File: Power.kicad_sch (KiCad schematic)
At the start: 1 part, among them J901 Conn_01x02

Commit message: Fix schematic ERC errors
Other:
- sheet Supercaps ports: added Vscap; removed Vcap
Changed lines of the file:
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@@
 		)
 	)
-	(hierarchical_label "Vcap"
+	(hierarchical_label "Vscap"
 		(shape output)
 		(at 146.05 31.75 0)
@@
 			)
 		)
-		(property "Sim.Enable" ""
-			(at 34.29 39.37 0)
-			(effects
-				(font
-					(size 1.27 1.27)
-				)
-			)
-		)
 		(pin "1"
 		)
@@
 			)
 		)
-		(pin "Vcap" bidirectional
+		(pin "Vscap" bidirectional
 			(at 143.51 68.58 180)
 			(effects

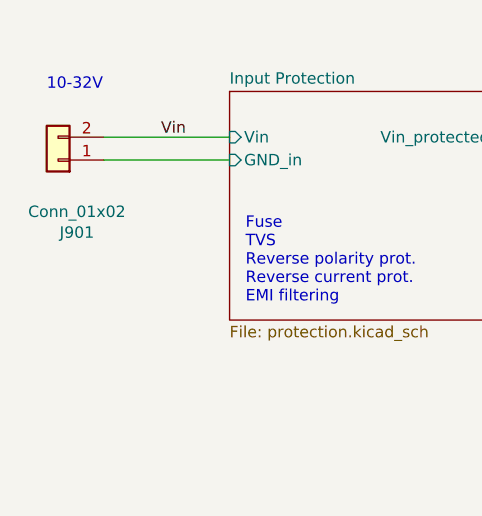
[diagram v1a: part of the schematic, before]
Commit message: Reannotate components
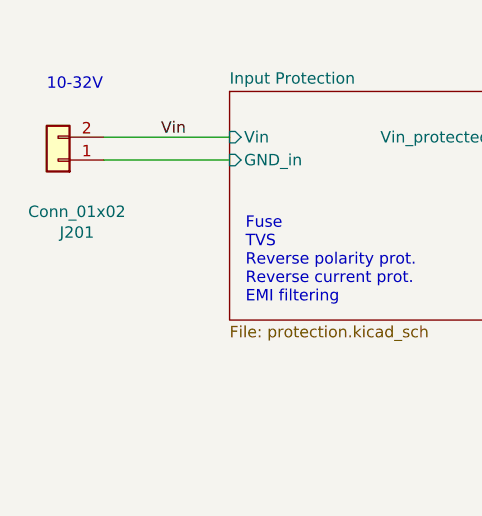
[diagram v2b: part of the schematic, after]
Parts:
- renumbered J901 to J201
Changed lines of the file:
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@@
 		(on_board yes)
 		(dnp no)
-		(property "Reference" "#PWR0901"
+		(property "Reference" "#PWR0201"
 			(at 215.9 36.83 0)
 			(effects
@@
 			(project "Yellow"
 				(path "/abc482bd-3f17-4d35-80db-1da3dcdb5c27/c7bf4e1f-6bd1-4be7-9e56-1bd438bf5d42"
-					(reference "#PWR0901")
+					(reference "#PWR0201")
 					(unit 1)
 				)
@@
 		(on_board yes)
 		(dnp no)
-		(property "Reference" "J901"
+		(property "Reference" "J201"
 			(at 36.3728 47.4218 0)
 			(effects
@@
 			(project "Yellow"
 				(path "/abc482bd-3f17-4d35-80db-1da3dcdb5c27/c7bf4e1f-6bd1-4be7-9e56-1bd438bf5d42"
-					(reference "J901")
+					(reference "J201")
 					(unit 1)
 				)
@@
 		(dnp no)
 		(fields_autoplaced yes)
-		(property "Reference" "#PWR0902"
+		(property "Reference" "#PWR0202"
 			(at 215.9 69.85 0)
 			(effects
@@
 			(project ""
 				(path "/abc482bd-3f17-4d35-80db-1da3dcdb5c27/c7bf4e1f-6bd1-4be7-9e56-1bd438bf5d42"
-					(reference "#PWR0902")
+					(reference "#PWR0202")
 					(unit 1)
 				)
@@
 			(project "HALPI2"
 				(path "/abc482bd-3f17-4d35-80db-1da3dcdb5c27/c7bf4e1f-6bd1-4be7-9e56-1bd438bf5d42"
-					(page "14")
+					(page "5")
 				)
 			)
@@
 			(project "HALPI2"
 				(path "/abc482bd-3f17-4d35-80db-1da3dcdb5c27/c7bf4e1f-6bd1-4be7-9e56-1bd438bf5d42"
-					(page "15")
+					(page "10")
 				)
 			)
@@
 			(project "HALPI2"
 				(path "/abc482bd-3f17-4d35-80db-1da3dcdb5c27/c7bf4e1f-6bd1-4be7-9e56-1bd438bf5d42"
-					(page "13")
+					(page "4")
 				)
 			)
@@
 			(project "HALPI2"
 				(path "/abc482bd-3f17-4d35-80db-1da3dcdb5c27/c7bf4e1f-6bd1-4be7-9e56-1bd438bf5d42"
-					(page "12")
+					(page "3")
 				)
 			)
@@
 			(project "HALPI2"
 				(path "/abc482bd-3f17-4d35-80db-1da3dcdb5c27/c7bf4e1f-6bd1-4be7-9e56-1bd438bf5d42"
-					(page "16")
-				)
-			)
+					(page "11")
+				)
+			)

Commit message: Further refinements
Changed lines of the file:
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@@
 		)
 	)
-	(hierarchical_label "EN5V"
+	(hierarchical_label "VCCEN"
 		(shape input)
 		(at 184.15 73.66 180)
@@
 		)
 	)
-	(hierarchical_label "EN5V"
+	(hierarchical_label "VCCEN"
 		(shape input)
 		(at 184.15 40.64 180)
@@
 			)
 		)
+		(property "LCSC Part" ""
+			(at 34.29 39.37 0)
+			(effects
+				(font
+					(size 1.27 1.27)
+				)
+			)
+		)
+		(property "Sim.Enable" ""
+			(at 34.29 39.37 0)
+			(effects
+				(font
+					(size 1.27 1.27)
+				)
+			)
+		)

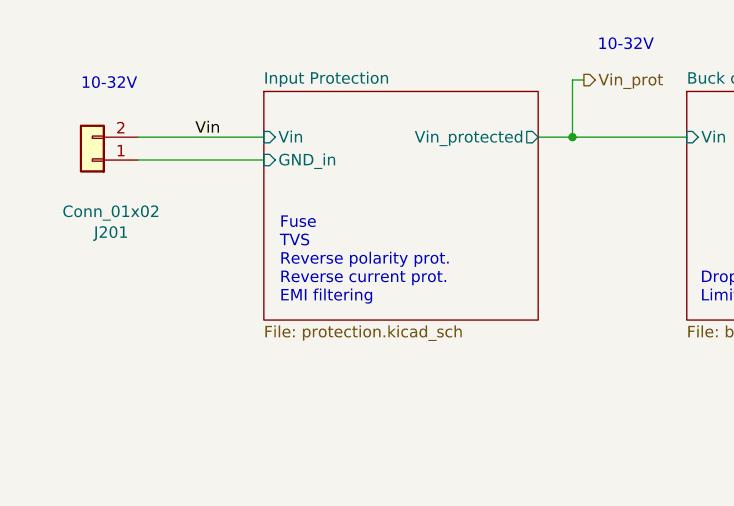
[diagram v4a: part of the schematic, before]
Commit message: Change MCU to RP2040
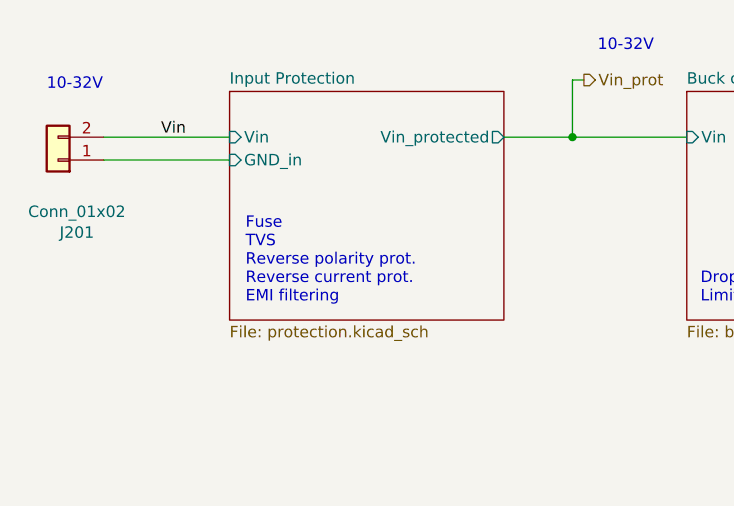
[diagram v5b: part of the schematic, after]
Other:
- moved on the sheet: J201
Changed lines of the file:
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@@
 	(text "10-32V"
 		(exclude_from_sim no)
-		(at 33.02 31.75 0)
+		(at 29.21 31.75 0)
 		(effects
 			(font
@@
 	(text "Fuse\nTVS\nReverse polarity prot.\nReverse current prot.\nEMI filtering"
 		(exclude_from_sim no)
-		(at 55.118 55.372 0)
+		(at 51.308 55.372 0)
 		(effects
 			(font
@@
 	(wire
 		(pts
-			(xy 39.37 36.83) (xy 53.34 36.83)
+			(xy 35.56 36.83) (xy 49.53 36.83)
 		)
 		(stroke
@@
 	(wire
 		(pts
-			(xy 83.82 36.83) (xy 87.63 36.83)
+			(xy 80.01 36.83) (xy 87.63 36.83)
 		)
 		(stroke
@@
 	(wire
 		(pts
-			(xy 39.37 39.37) (xy 53.34 39.37)
+			(xy 35.56 39.37) (xy 49.53 39.37)
 		)
 		(stroke
@@
 	)
 	(label "Vin"
-		(at 45.72 36.83 0)
+		(at 41.91 36.83 0)
 		(effects
 			(font
@@
 	(symbol
 		(lib_id "Connector_Generic:Conn_01x02")
-		(at 34.29 39.37 180)
+		(at 30.48 39.37 180)
 		(unit 1)
 		(exclude_from_sim no)
@@
 		(dnp no)
 		(property "Reference" "J201"
-			(at 36.3728 47.4218 0)
+			(at 32.5628 47.4218 0)
 			(effects
 				(font
@@
 		)
 		(property "Value" "Conn_01x02"
-			(at 36.3728 45.1104 0)
+			(at 32.5628 45.1104 0)
 			(effects
 				(font
@@
 		)
 		(property "Footprint" "Connector_Phoenix_MC:PhoenixContact_MCV_1,5_2-G-3.81_1x02_P3.81mm_Vertical"
-			(at 34.29 39.37 0)
+			(at 30.48 39.37 0)
 			(effects
 				(font
@@
 		)
 		(property "Datasheet" "~"
-			(at 34.29 39.37 0)
+			(at 30.48 39.37 0)
 			(effects
 				(font
@@
 		)
 		(property "Description" "Generic connector, single row, 01x02, script generated (kicad-library-utils/schlib/autogen/connector/)"
-			(at 34.29 39.37 0)
+			(at 30.48 39.37 0)
 			(effects
 				(font
@@
 		)
 		(property "LCSC" "C8396"
-			(at 34.29 39.37 0)
+			(at 30.48 39.37 0)
 			(effects
 				(font
@@
 		)
 		(property "JLCPCB_CORRECTION" ""
-			(at 34.29 39.37 0)
+			(at 30.48 39.37 0)
 			(effects
 				(font
@@
 		)
 		(property "Characteristics" ""
-			(at 34.29 39.37 0)
+			(at 30.48 39.37 0)
 			(effects
 				(font
@@
 		)
 		(property "LCSC Part" ""
-			(at 34.29 39.37 0)
+			(at 30.48 39.37 0)
 			(effects
 				(font
@@
 		)
 		(property "Sim.Enable" ""
-			(at 34.29 39.37 0)
+			(at 30.48 39.37 0)
 			(effects
 				(font
@@
 	)
 	(sheet
-		(at 53.34 31.75)
+		(at 49.53 31.75)
 		(size 30.48 25.4)
 		(exclude_from_sim no)
@@
 		)
 		(property "Sheetname" "Input Protection"
-			(at 53.34 31.0384 0)
+			(at 49.53 31.0384 0)
 			(effects
 				(font
@@
 		)
 		(property "Sheetfile" "protection.kicad_sch"
-			(at 53.34 57.7346 0)
+			(at 49.53 57.7346 0)
 			(effects
 				(font
@@
 		)
 		(pin "Vin_protected" output
-			(at 83.82 36.83 0)
+			(at 80.01 36.83 0)
 			(effects
 				(font
@@
 		)
 		(pin "Vin" input
-			(at 53.34 36.83 180)
+			(at 49.53 36.83 180)
 			(effects
 				(font
@@
 		)
 		(pin "GND_in" input
-			(at 53.34 39.37 180)
-			(effects
-				(font
+			(at 49.53 39.37 180)
+			(effects
+				(font

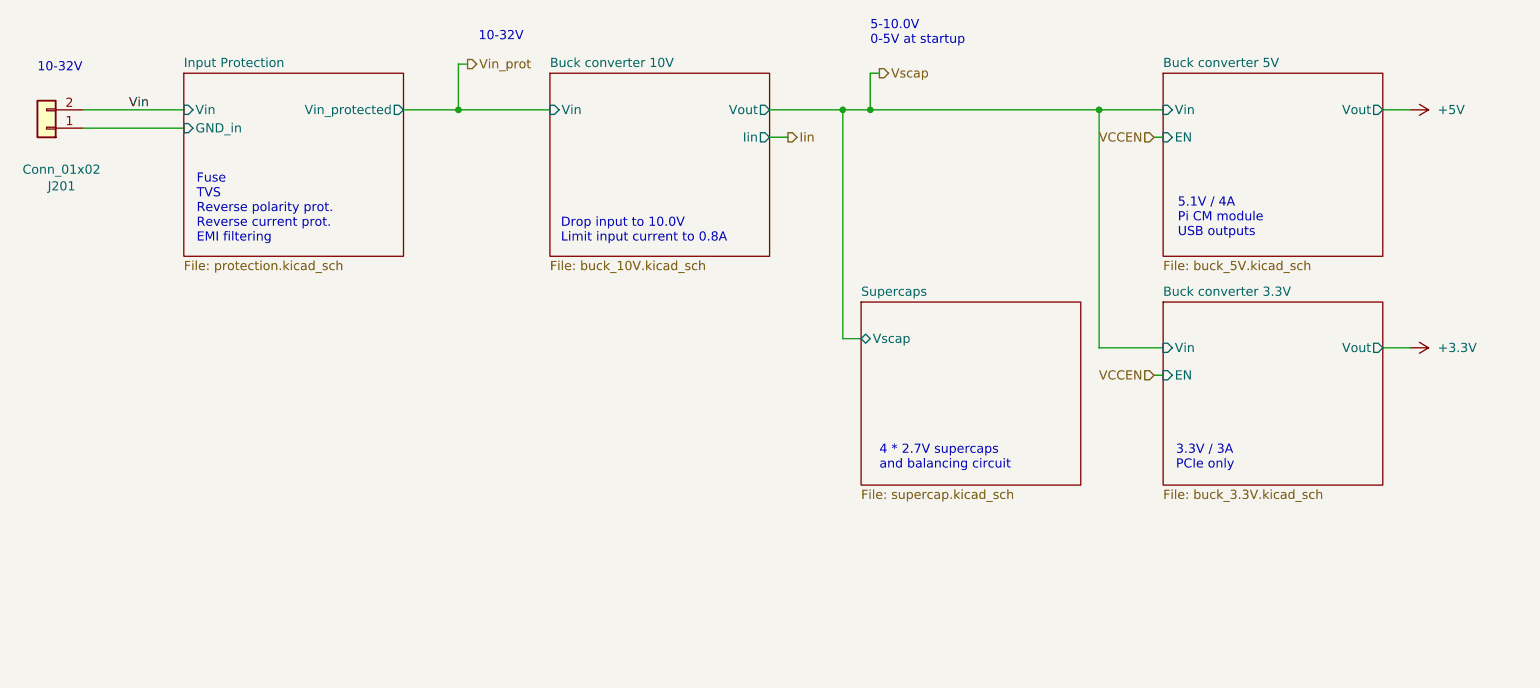
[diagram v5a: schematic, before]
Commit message: Finish transitioning to RP2040
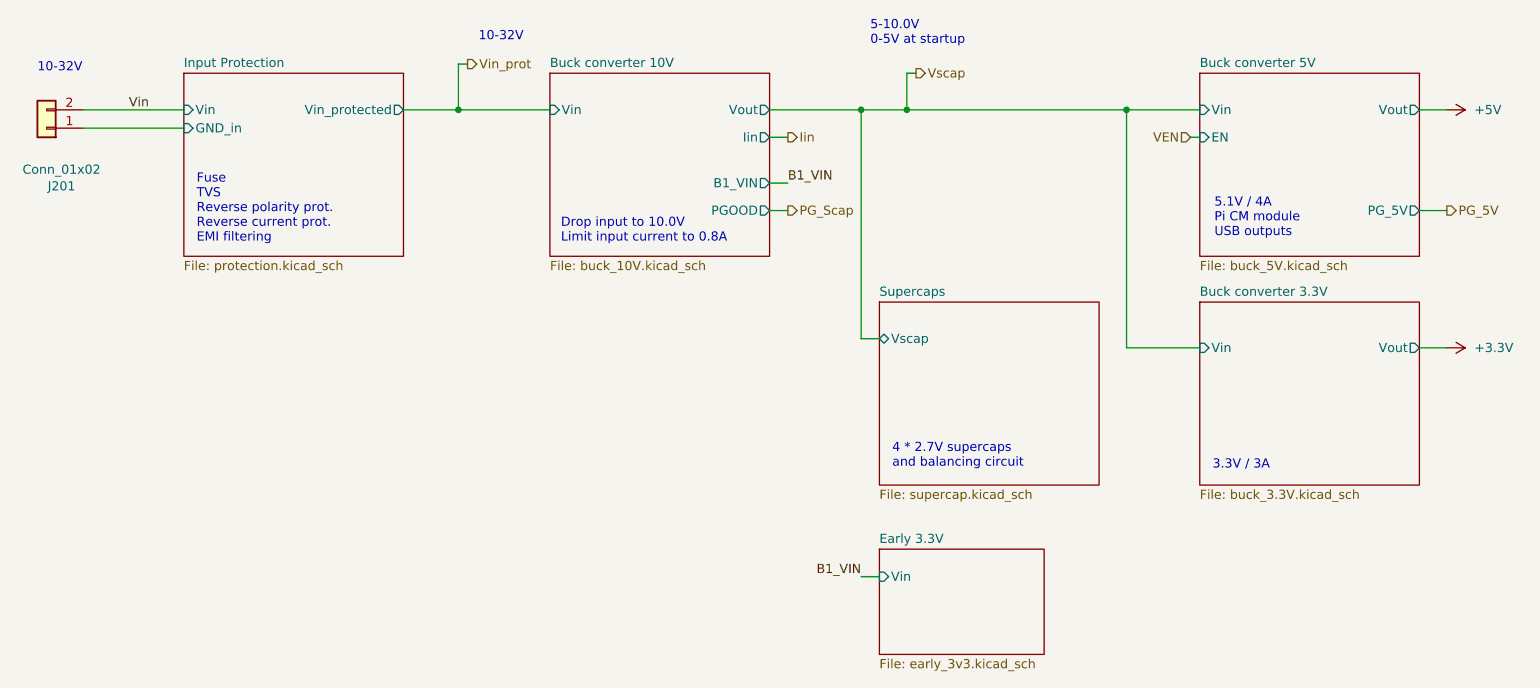
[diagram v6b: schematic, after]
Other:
- added sheet Early 3.3V (early_3v3.kicad_sch)
- sheet Buck converter 10V ports: added B1_VIN, PGOOD; removed none
- sheet Buck converter 3.3V ports: added none; removed EN
- sheet Buck converter 5V ports: added PG_5V; removed none
- note added: "3.3V / 3A"
- note removed: "3.3V / 3A PCIe only"

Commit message: Apply part PCBA position corrections
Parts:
- J201: JLCPCB_CORRECTION (none) -> 1.905;0;180
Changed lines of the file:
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@@
 			)
 		)
-		(property "JLCPCB_CORRECTION" ""
+		(property "JLCPCB_CORRECTION" "1.905;0;180"
 			(at 30.48 39.37 0)
 			(effects
